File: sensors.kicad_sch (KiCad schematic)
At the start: 43 parts, among them J12 RF Antenna, J5 Micro_SD_Card, U10 SHT45-AD1B-R2, U11 RFM95W-915S2, U12 W25Q128JVSIQ, U16 PCA9685BS, U5 SAM-M10Q-00B, U6 MS860702BA01-50, U7 DPS310, U8 H3LIS331DL, U9 LSM6DSO32TR

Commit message: updated footprint library
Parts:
- BT1: footprint (none) -> Battery:BatteryHolder_Bulgin_BX0036_1xC
- C11, C12, C13, C14, C15, C16, C17, C18, C19, C20, C21, C22, C31: footprint Capacitor_SMD:C_0201_0603Metric -> Capacitor_SMD:C_0402_1005Metric
- C23, C29, C36: footprint Capacitor_SMD:C_0201_0603Metric -> Capacitor_SMD:C_0603_1608Metric
- R11, R12, R13, R14, R15, R16, R17, R18, R19, R20, R21, R24, R32: footprint Resistor_SMD:R_0201_0603Metric -> Resistor_SMD:R_0402_1005Metric
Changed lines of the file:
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@@
       (effects (font (size 1.27 1.27)))
     )
-    (property "Footprint" "Resistor_SMD:R_0201_0603Metric" (at 156.21 52.832 90)
+    (property "Footprint" "Resistor_SMD:R_0402_1005Metric" (at 156.21 52.832 90)
       (effects (font (size 1.27 1.27)) hide)
     )
@@
       (effects (font (size 1.27 1.27)) (justify left))
     )
-    (property "Footprint" "Resistor_SMD:R_0201_0603Metric" (at 132.842 163.83 90)
+    (property "Footprint" "Resistor_SMD:R_0402_1005Metric" (at 132.842 163.83 90)
       (effects (font (size 1.27 1.27)) hide)
     )
@@
       (effects (font (size 1.27 1.27)) (justify left))
     )
-    (property "Footprint" "Capacitor_SMD:C_0201_0603Metric" (at 275.2852 160.02 0)
+    (property "Footprint" "Capacitor_SMD:C_0402_1005Metric" (at 275.2852 160.02 0)
       (effects (font (size 1.27 1.27)) hide)
     )
@@
       (effects (font (size 1.27 1.27)) (justify left))
     )
-    (property "Footprint" "Capacitor_SMD:C_0201_0603Metric" (at 276.5552 45.72 0)
+    (property "Footprint" "Capacitor_SMD:C_0603_1608Metric" (at 276.5552 45.72 0)
       (effects (font (size 1.27 1.27)) hide)
     )
@@
       (effects (font (size 1.27 1.27)) (justify left))
     )
-    (property "Footprint" "Capacitor_SMD:C_0201_0603Metric" (at 276.5552 85.09 0)
+    (property "Footprint" "Capacitor_SMD:C_0402_1005Metric" (at 276.5552 85.09 0)
       (effects (font (size 1.27 1.27)) hide)
     )
@@
       (effects (font (size 1.27 1.27)))
     )
-    (property "Footprint" "Resistor_SMD:R_0201_0603Metric" (at 156.21 32.512 90)
+    (property "Footprint" "Resistor_SMD:R_0402_1005Metric" (at 156.21 32.512 90)
       (effects (font (size 1.27 1.27)) hide)
     )
@@
       (effects (font (size 1.27 1.27)) (justify left))
     )
-    (property "Footprint" "Capacitor_SMD:C_0201_0603Metric" (at 160.9852 48.26 0)
+    (property "Footprint" "Capacitor_SMD:C_0603_1608Metric" (at 160.9852 48.26 0)
       (effects (font (size 1.27 1.27)) hide)
     )
@@
       (effects (font (size 1.27 1.27)) (justify left))
     )
-    (property "Footprint" "Capacitor_SMD:C_0201_0603Metric" (at 61.9252 109.22 0)
+    (property "Footprint" "Capacitor_SMD:C_0402_1005Metric" (at 61.9252 109.22 0)
       (effects (font (size 1.27 1.27)) hide)
     )
@@
       (effects (font (size 1.27 1.27)) (justify left))
     )
-    (property "Footprint" "Capacitor_SMD:C_0201_0603Metric" (at 127.9652 48.26 0)
+    (property "Footprint" "Capacitor_SMD:C_0402_1005Metric" (at 127.9652 48.26 0)
       (effects (font (size 1.27 1.27)) hide)
     )
@@
       (effects (font (size 1.27 1.27)) (justify left))
     )
-    (property "Footprint" "Resistor_SMD:R_0201_0603Metric" (at 125.222 104.14 90)
+    (property "Footprint" "Resistor_SMD:R_0402_1005Metric" (at 125.222 104.14 90)
       (effects (font (size 1.27 1.27)) hide)
     )
@@
       (effects (font (size 1.27 1.27)) (justify left))
     )
-    (property "Footprint" "Capacitor_SMD:C_0201_0603Metric" (at 83.5152 109.22 0)
+    (property "Footprint" "Capacitor_SMD:C_0402_1005Metric" (at 83.5152 109.22 0)
       (effects (font (size 1.27 1.27)) hide)
     )
@@
       (effects (font (size 1.27 1.27)))
     )
-    (property "Footprint" "Resistor_SMD:R_0201_0603Metric" (at 128.778 36.83 90)
+    (property "Footprint" "Resistor_SMD:R_0402_1005Metric" (at 128.778 36.83 90)
       (effects (font (size 1.27 1.27)) hide)
     )
@@
       (effects (font (size 1.27 1.27)) (justify left))
     )
-    (property "Footprint" "Capacitor_SMD:C_0201_0603Metric" (at 33.9852 173.99 0)
+    (property "Footprint" "Capacitor_SMD:C_0402_1005Metric" (at 33.9852 173.99 0)
       (effects (font (size 1.27 1.27)) hide)
     )
@@
       (effects (font (size 1.27 1.27)) (justify left))
     )
-    (property "Footprint" "Resistor_SMD:R_0201_0603Metric" (at 250.952 156.21 90)
+    (property "Footprint" "Resistor_SMD:R_0402_1005Metric" (at 250.952 156.21 90)
       (effects (font (size 1.27 1.27)) hide)
     )
@@
       (effects (font (size 1.27 1.27)) (justify left))
     )
-    (property "Footprint" "Resistor_SMD:R_0201_0603Metric" (at 154.432 163.83 90)
+    (property "Footprint" "Resistor_SMD:R_0402_1005Metric" (at 154.432 163.83 90)
       (effects (font (size 1.27 1.27)) hide)
     )
@@
       (effects (font (size 1.27 1.27)))
     )
-    (property "Footprint" "Resistor_SMD:R_0201_0603Metric" (at 60.96 52.578 90)
+    (property "Footprint" "Resistor_SMD:R_0402_1005Metric" (at 60.96 52.578 90)
       (effects (font (size 1.27 1.27)) hide)
     )
@@
       (effects (font (size 1.27 1.27)) (justify left))
     )
-    (property "Footprint" "Capacitor_SMD:C_0201_0603Metric" (at 276.5552 110.49 0)
+    (property "Footprint" "Capacitor_SMD:C_0402_1005Metric" (at 276.5552 110.49 0)
       (effects (font (size 1.27 1.27)) hide)
     )
@@
       (effects (font (size 1.27 1.27)) (justify left))
     )
-    (property "Footprint" "Resistor_SMD:R_0201_0603Metric" (at 151.892 182.88 90)
+    (property "Footprint" "Resistor_SMD:R_0402_1005Metric" (at 151.892 182.88 90)
       (effects (font (size 1.27 1.27)) hide)
     )
@@
       (effects (font (size 1.27 1.27)) (justify left))
     )
-    (property "Footprint" "Capacitor_SMD:C_0201_0603Metric" (at 64.4652 173.99 0)
+    (property "Footprint" "Capacitor_SMD:C_0402_1005Metric" (at 64.4652 173.99 0)
       (effects (font (size 1.27 1.27)) hide)
     )
@@
       (effects (font (size 1.27 1.27)) (justify left))
     )
-    (property "Footprint" "Resistor_SMD:R_0201_0603Metric" (at 31.242 102.87 90)
+    (property "Footprint" "Resistor_SMD:R_0402_1005Metric" (at 31.242 102.87 90)
       (effects (font (size 1.27 1.27)) hide)
     )
@@
       (effects (font (size 1.27 1.27)) (justify left))
     )
-    (property "Footprint" "Capacitor_SMD:C_0201_0603Metric" (at 96.2152 44.45 0)
+    (property "Footprint" "Capacitor_SMD:C_0402_1005Metric" (at 96.2152 44.45 0)
       (effects (font (size 1.27 1.27)) hide)
     )
@@
       (effects (font (size 1.27 1.27)) (justify left))
     )
-    (property "Footprint" "Capacitor_SMD:C_0201_0603Metric" (at 111.4552 44.45 0)
+    (property "Footprint" "Capacitor_SMD:C_0402_1005Metric" (at 111.4552 44.45 0)
       (effects (font (size 1.27 1.27)) hide)
     )
@@
       (effects (font (size 1.27 1.27)) (justify left))
     )
-    (property "Footprint" "Capacitor_SMD:C_0201_0603Metric" (at 186.3852 110.49 0)
+    (property "Footprint" "Capacitor_SMD:C_0402_1005Metric" (at 186.3852 110.49 0)
       (effects (font (size 1.27 1.27)) hide)
     )
@@
       (effects (font (size 1.27 1.27)) (justify left))
     )
-    (property "Footprint" "Resistor_SMD:R_0201_0603Metric" (at 93.472 172.72 90)
+    (property "Footprint" "Resistor_SMD:R_0402_1005Metric" (at 93.472 172.72 90)
       (effects (font (size 1.27 1.27)) hide)
     )
@@
       (effects (font (size 1.27 1.27)) (justify left))
     )
-    (property "Footprint" "Capacitor_SMD:C_0201_0603Metric" (at 134.3152 189.23 0)
+    (property "Footprint" "Capacitor_SMD:C_0603_1608Metric" (at 134.3152 189.23 0)
       (effects (font (size 1.27 1.27)) hide)
     )
@@
       (effects (font (size 1.27 1.27)) (justify left) hide)
     )
-    (property "Footprint" "" (at 132.08 44.196 90)
+    (property "Footprint" "Battery:BatteryHolder_Bulgin_BX0036_1xC" (at 132.08 44.196 90)
       (effects (font (size 1.27 1.27)) hide)
     )
@@
       (effects (font (size 1.27 1.27)))
     )
-    (property "Footprint" "Resistor_SMD:R_0201_0603Metric" (at 60.96 46.482 90)
+    (property "Footprint" "Resistor_SMD:R_0402_1005Metric" (at 60.96 46.482 90)
       (effects (font (size 1.27 1.27)) hide)
     )
@@
       (effects (font (size 1.27 1.27)) (justify left))
     )
-    (property "Footprint" "Capacitor_SMD:C_0201_0603Metric" (at 160.9852 110.49 0)
+    (property "Footprint" "Capacitor_SMD:C_0402_1005Metric" (at 160.9852 110.49 0)
       (effects (font (size 1.27 1.27)) hide)
     )
@@
       (effects (font (size 1.27 1.27)))
     )
-    (property "Footprint" "Resistor_SMD:R_0201_0603Metric" (at 80.518 33.02 90)
+    (property "Footprint" "Resistor_SMD:R_0402_1005Metric" (at 80.518 33.02 90)
       (effects (font (size 1.27 1.27)) hide)
     )
@@
       (effects (font (size 1.27 1.27)) (justify left))
     )
-    (property "Footprint" "Capacitor_SMD:C_0201_0603Metric" (at 49.2252 173.99 0)
-      (effects (font (size 1.27 1.27)) hide)
-    )
+    (property "Footprint" "Capacitor_SMD:C_0402_1005Metric" (at 49.2252 173.99 0)
+      (effects (font (size 1.27 1.27)) hide)
+    )

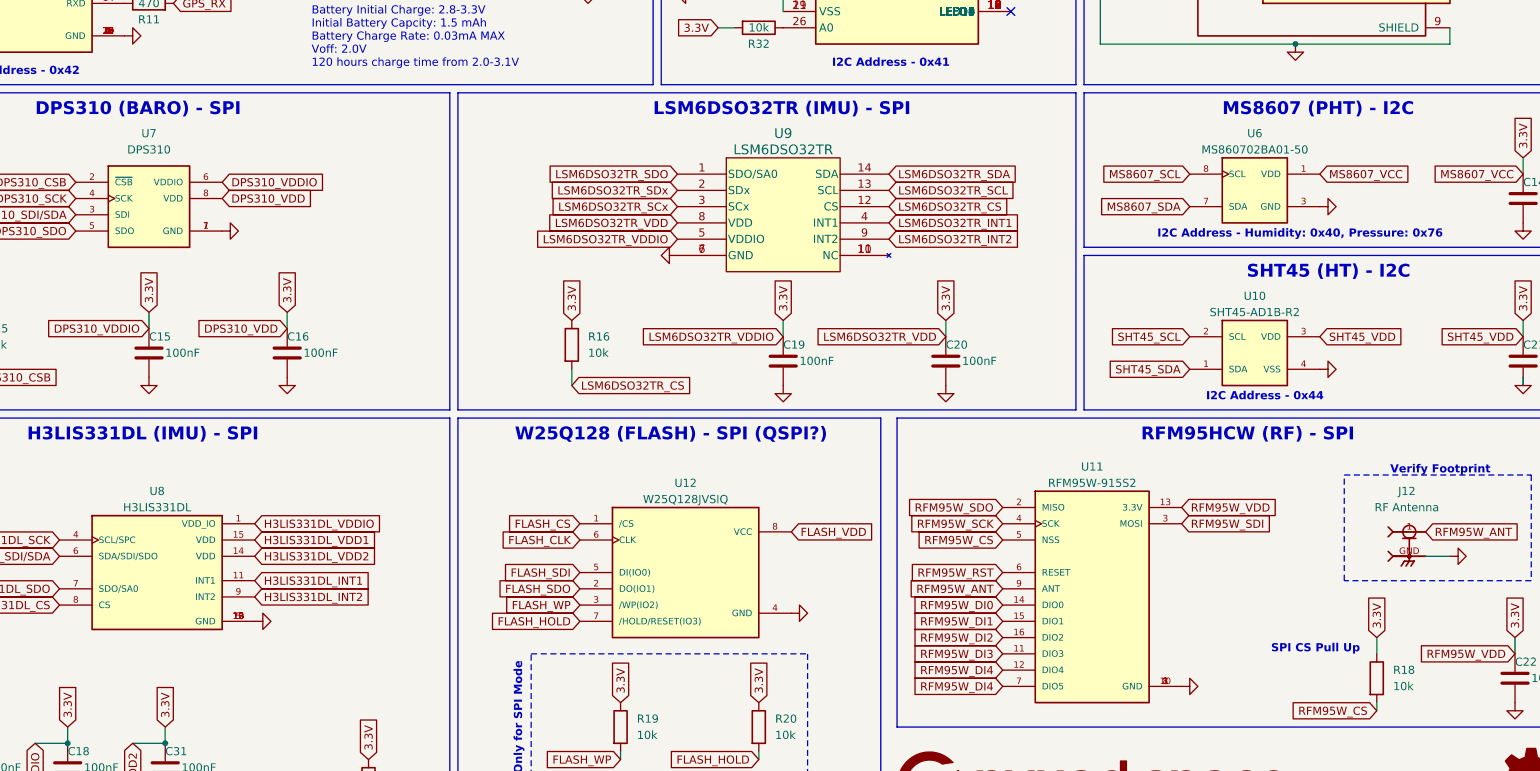
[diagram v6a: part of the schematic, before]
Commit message: Updated symbol footprints
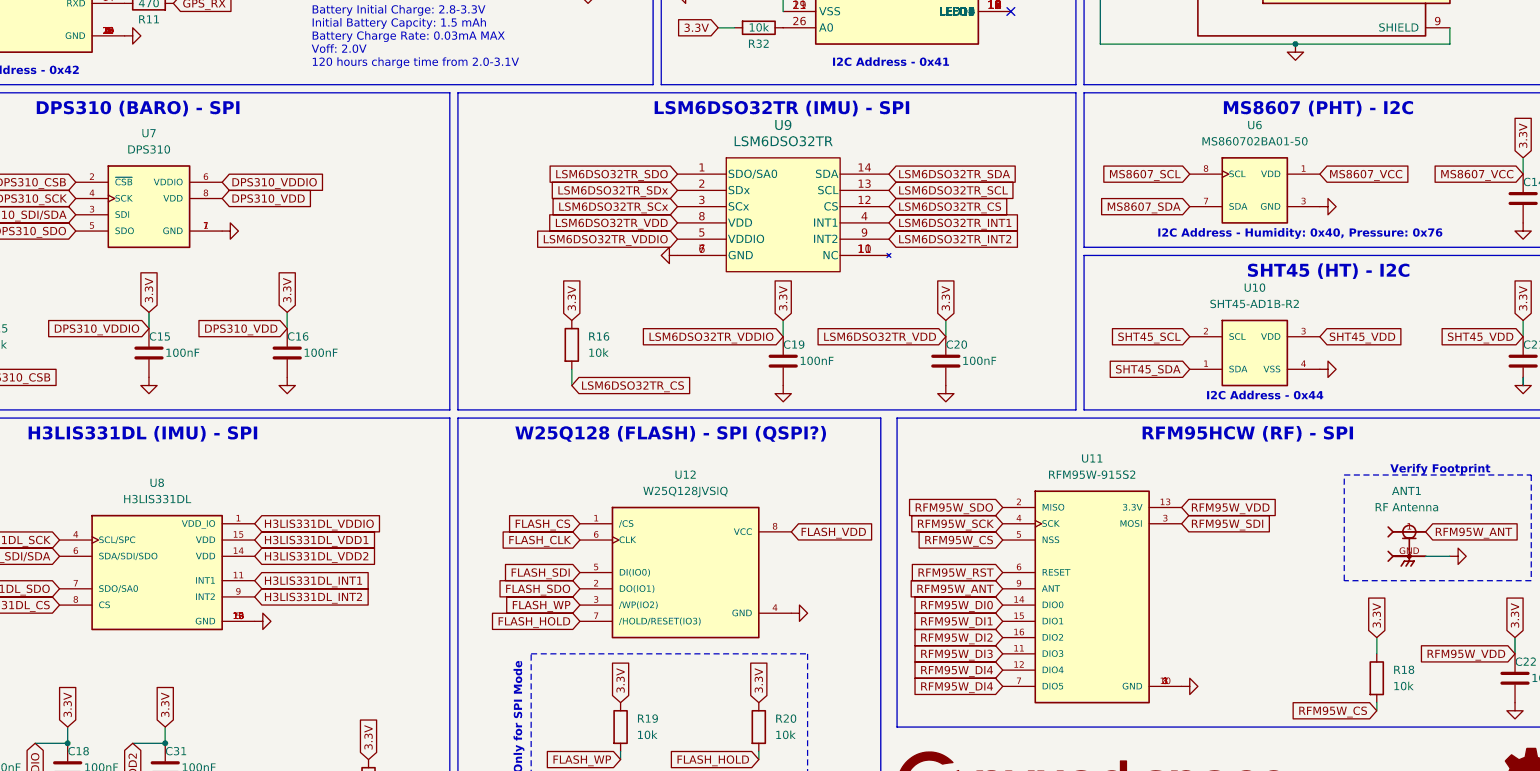
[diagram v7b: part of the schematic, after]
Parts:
- ANT1: renamed from J12; footprint TE_5449692-1 -> 5449692-1:TE_5449692-1
- C14: footprint Capacitor_SMD:C_0402_1005Metric -> Capacitor_SMD:C_0603_1608Metric
- D2: footprint (none) -> Diode_SMD:D_SOD-323
- D3: footprint LED_SMD:LED_0201_0603Metric -> LED_SMD:LED_0603_1608Metric
- R11, R12, R13, R14, R15, R16, R17, R18, R19, R20, R21, R24, R32: footprint Resistor_SMD:R_0402_1005Metric -> Resistor_SMD:R_0603_1608Metric

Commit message: updated schematic
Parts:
- removed J5: Micro_SD_Card, symbol Connector:Micro_SD_Card
- added SD1: MEM2067-02-180-00-A_REVB, MEM2067-02-180-00-A_REVB:GCT_MEM2067-02-180-00-A_REVB, symbol MEM2067-02-180-00-A_REVB:MEM2067-02-180-00-A_REVB
- BT?: renamed from BT1; footprint Battery:BatteryHolder_Bulgin_BX0036_1xC -> ML414H_IV01E:SEIKO_ML414H_IV01E
- renumbered C22 to C?, C29 to C?, C14 to C?, C36 to C?, C15 to C?, C13 to C?, C16 to C?, C17 to C?, C21 to C?, C31 to C?, C11 to C?, C12 to C?, C20 to C?, C23 to C?, C19 to C?, C18 to C?, D3 to D?, D2 to D?, R32 to R?, R19 to R?, R24 to R?, R16 to R?, R13 to R?, R18 to R?, R20 to R?, R11 to R?, R21 to R?, R15 to R?, R17 to R?, R12 to R?, R14 to R?, U12 to U?, U7 to U?, U9 to U?, U10 to U?, U11 to U?, U6 to U?, U5 to U?, U8 to U?, U16 to U?
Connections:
- net 3.3V: now also SD1.4 (VDD)
- net GND: now also SD1.10 (SHIELD), SD1.11 (SHIELD), SD1.12 (SHIELD), SD1.6 (VSS), SD1.9 (SHIELD)
- net SD_CS: now also SD1.2 (CD/DAT3)
- net SD_SCK: now also SD1.5 (CLK)
- net SD_SDI: now also SD1.3 (CMD)
- net SD_SDO: now also SD1.7 (DAT0)
